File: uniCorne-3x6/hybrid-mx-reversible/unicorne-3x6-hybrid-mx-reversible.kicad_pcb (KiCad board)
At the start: 2 copper layers, 133.8 x 91.4 mm, 98 parts, among them J1 MJ-4PP-9, J2 Nice!View, J3 Conn_01x02, J4 Conn_01x03, SW1 SW_MX_HS, SW10 SW_MX_HS, SW11 SW_MX_HS, SW12 SW_MX_HS, SW13 SW_MX_HS, SW14 SW_MX_HS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

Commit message: Amended hybrid 3x6
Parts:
- U1: footprint TB2086_MISC:ProMicro-ish-dn-rev-unrouted_3x5 -> TB2086_MISC:ProMicro-ish-dn-rev-unrouted_3x6
- moved R3 1.32 mm to (184.7, 109.9)
- moved R4 1.32 mm to (184.7, 111.8)
- moved JP9 0.76 mm to (188.6, 110.7)
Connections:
- PSW1 pad 1: unconnected-(PSW1-A-Pad1) -> BAT+
- PSW1 pad 3: BAT+ -> unconnected-(PSW1-C-Pad3)
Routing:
- net LED: track 60.3 -> 78.4 mm, vias 4 -> 5
- net unconnected-(U1-RAW-Pad24): track 28.3 -> 11.0 mm
- net unconnected-(PSW1-A-Pad1): track 6.66 -> 0.00 mm
- net unconnected-(PSW1-C-Pad3): track 0.00 -> 6.50 mm
- net SDA: track 71.4 -> 66.5 mm, vias 4 -> 5
- net col0: track 200.7 -> 197.3 mm, vias 1 -> 2
- net DATA: track 64.8 -> 67.7 mm
- net row0: track 138.1 -> 140.9 mm, vias 2 -> 3
- net row1: track 136.0 -> 138.4 mm, vias 2 -> 3
- net row3: track 89.5 -> 87.1 mm
- net GND: track 34.9 -> 36.9 mm, vias 16 -> 17
- net BAT+: track 16.1 -> 14.2 mm
- net col1: track 172.7 -> 170.8 mm, vias 1 -> 2
- net col5: track 154.9 -> 153.3 mm, vias 2 -> 3
- net Net-(JP9-C): track 15.4 -> 13.9 mm
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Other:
- board text added: "uniCorne Hybrid 3x6"
- board text removed: "uniCorne Hybrid"

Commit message: small tweak
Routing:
- net col0: track 197.3 -> 192.3 mm
- net DATA: track 67.7 -> 72.4 mm
- net RESET: track 59.1 -> 62.9 mm
- net SDA: track 66.5 -> 63.9 mm
- net SCL: track 58.7 -> 56.8 mm
- net col1: track 170.8 -> 169.2 mm
- net unconnected-(PSW1-C-Pad3): track 6.50 -> 5.34 mm
- net col5: track 153.3 -> 152.2 mm, vias 3 -> 2
- net VCC: track 584.3 -> 583.3 mm
- net GND: track 36.9 -> 35.9 mm
- net row2: track 159.0 -> 158.2 mm
- net row3: track 87.1 -> 86.6 mm

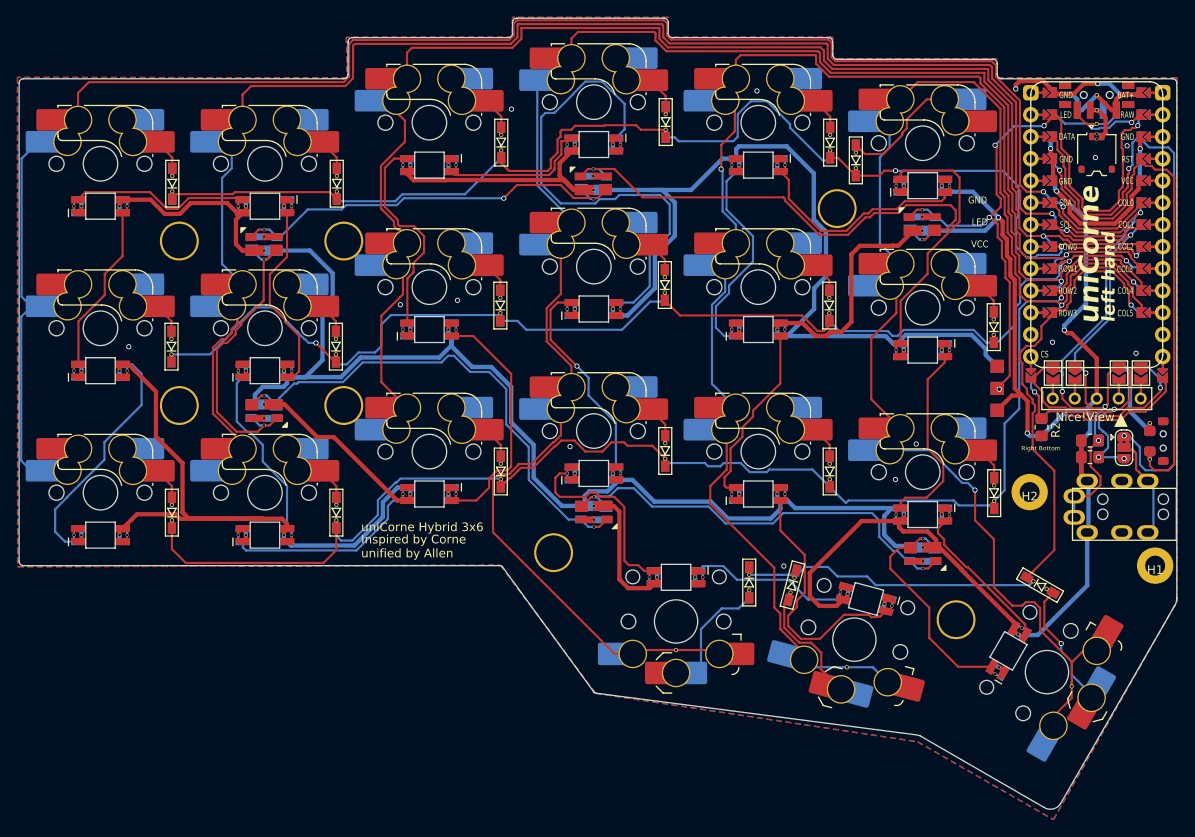
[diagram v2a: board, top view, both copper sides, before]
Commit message: amended footprint for LED
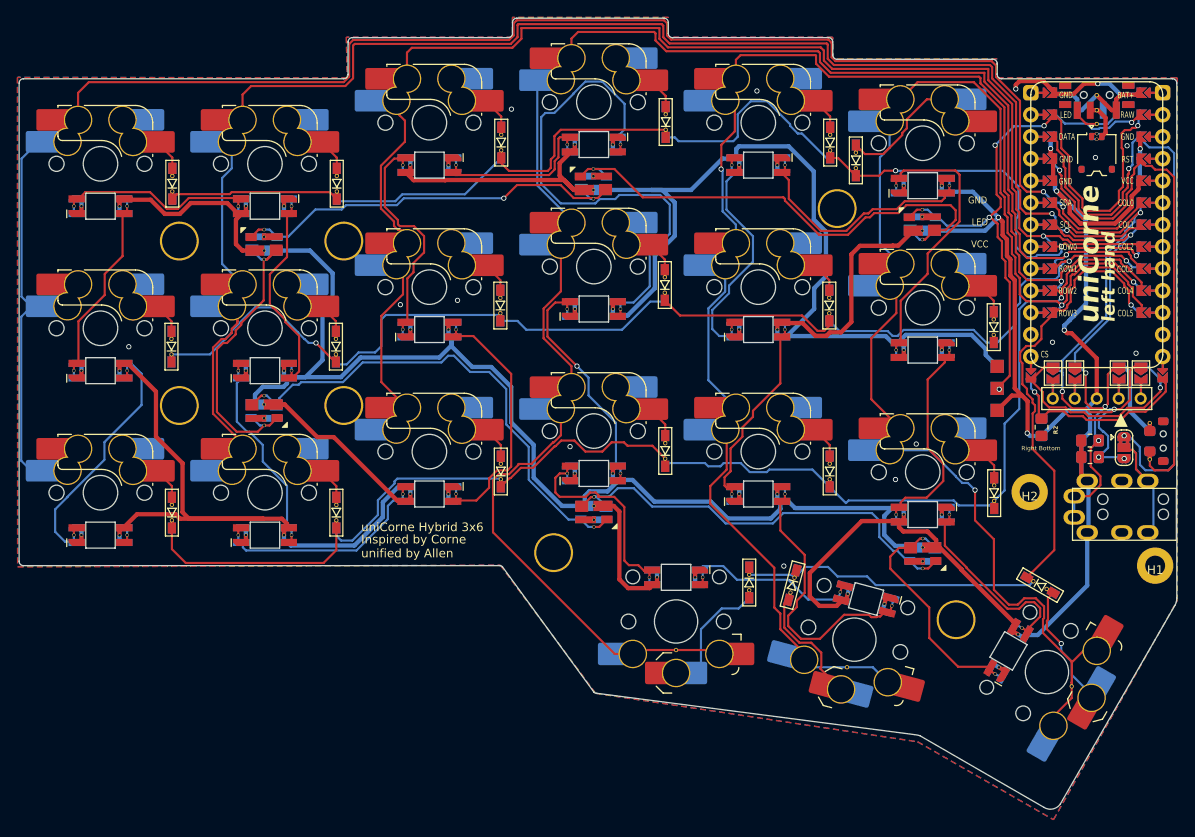
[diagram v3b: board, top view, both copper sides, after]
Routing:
- net VCC: track 583.3 -> 578.6 mm
- net Net-(L18-DIN): track 17.7 -> 20.6 mm
- net col5: track 152.2 -> 153.1 mm
- net Net-(L11-DIN): track 24.3 -> 25.0 mm
- net row0: track 140.9 -> 140.3 mm
- net Net-(L3-DIN): track 16.6 -> 17.2 mm

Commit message: small tweak
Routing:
- net row0: track 140.3 -> 141.2 mm
- net VCC: track 578.6 -> 577.9 mm
- net Net-(L26-DOUT): track 50.0 -> 49.3 mm

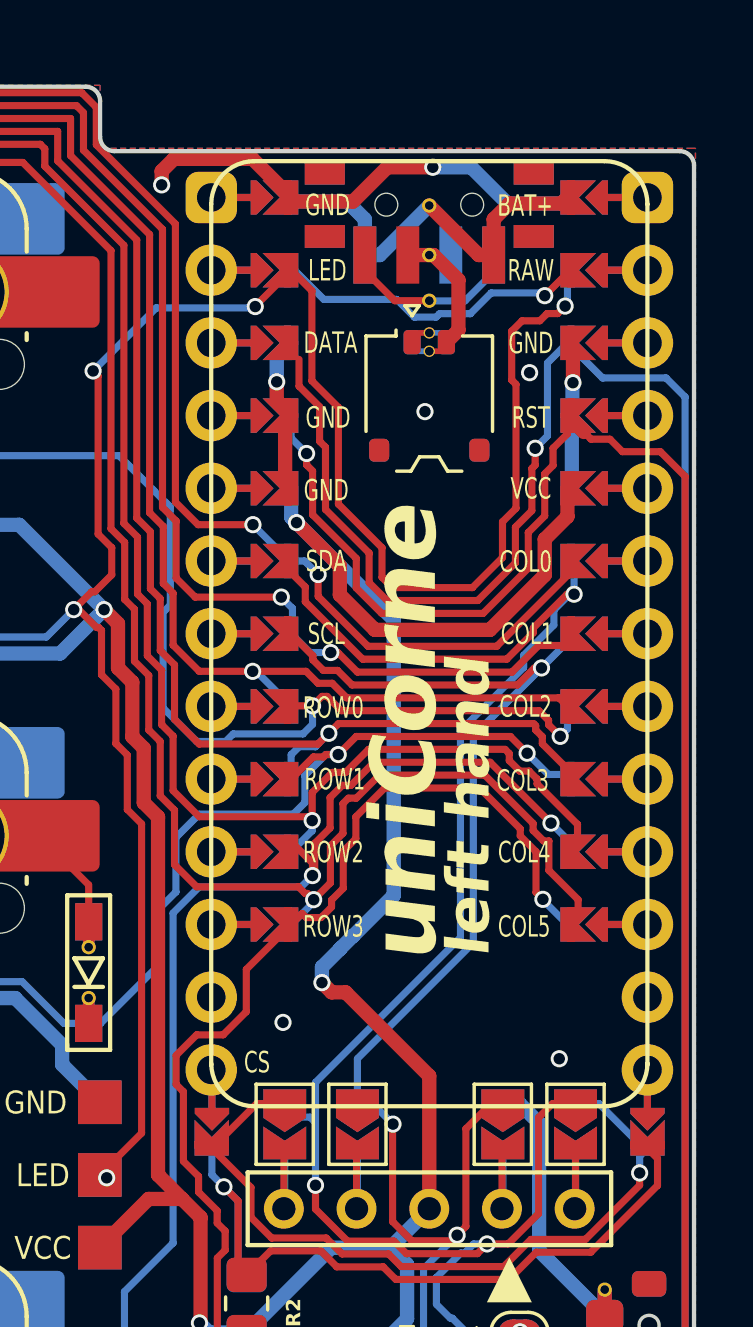
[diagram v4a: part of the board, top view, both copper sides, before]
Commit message: fixed footprint for promicro-ish 3x6
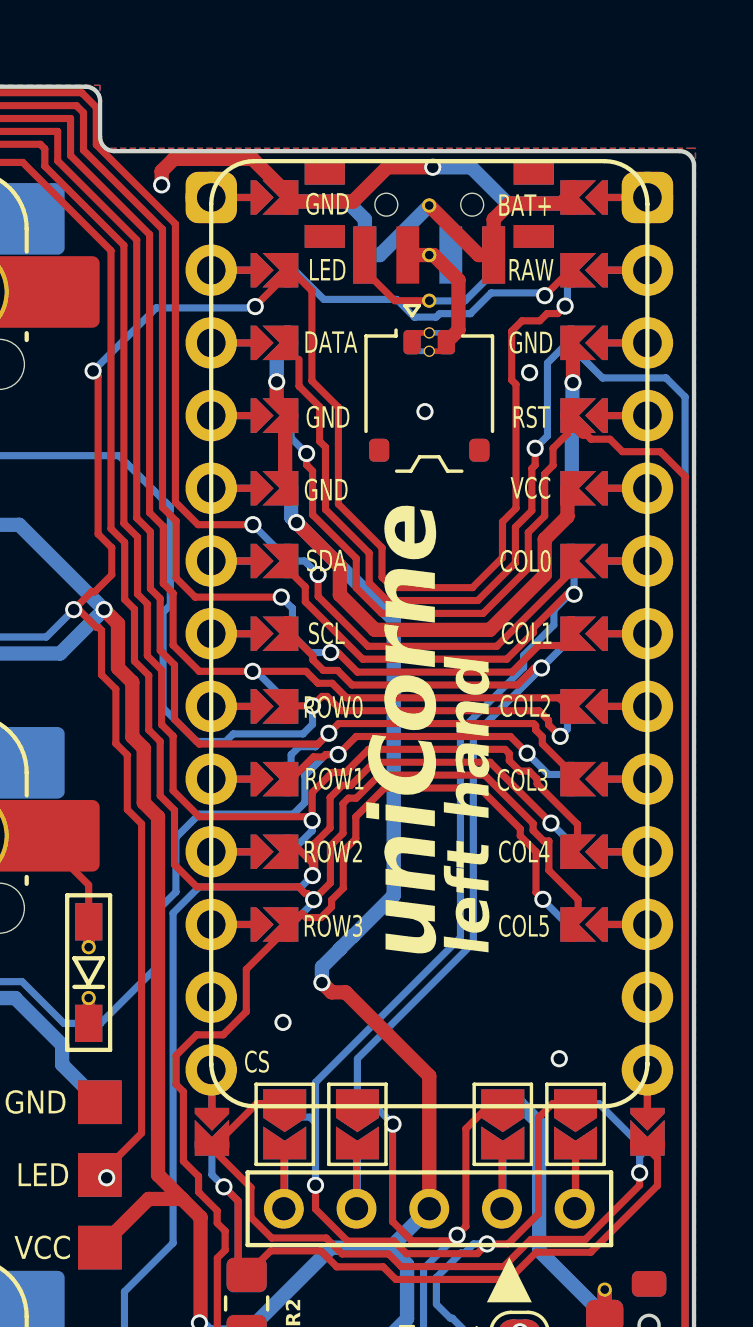
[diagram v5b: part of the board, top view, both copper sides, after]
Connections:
- U1 pad 12: IS_LEFT -> CS
- U1 pad 13: CS -> IS_LEFT
